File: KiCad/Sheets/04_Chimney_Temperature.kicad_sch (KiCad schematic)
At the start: 2 parts, among them U3 MAX6675

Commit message: Footprints are created and assigned
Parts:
- U3: footprint (none) -> Connector_PinSocket_2.54mm:PinSocket_1x05_P2.54mm_Vertical
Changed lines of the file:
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@@
 		(exclude_from_sim no)
 		(in_bom yes)
-		(on_board yes)
+		(on_board no)
 		(in_pos_files yes)
 		(dnp no)
@@
 			)
 		)
-		(property "Footprint" ""
+		(property "Footprint" "Connector_PinSocket_2.54mm:PinSocket_1x05_P2.54mm_Vertical"
 			(at 139.7 95.25 0)
 			(hide yes)

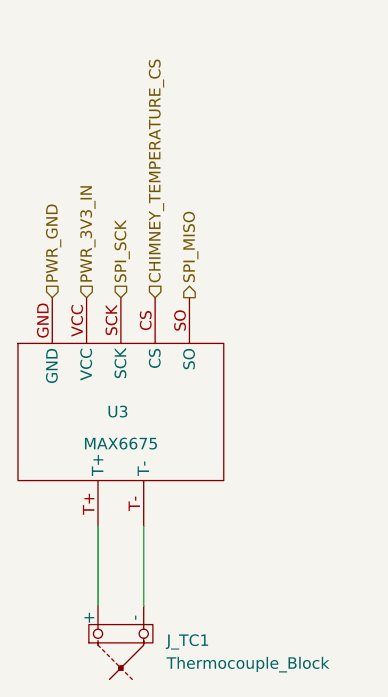
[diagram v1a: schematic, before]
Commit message: LEDs sheet added, schematic finished
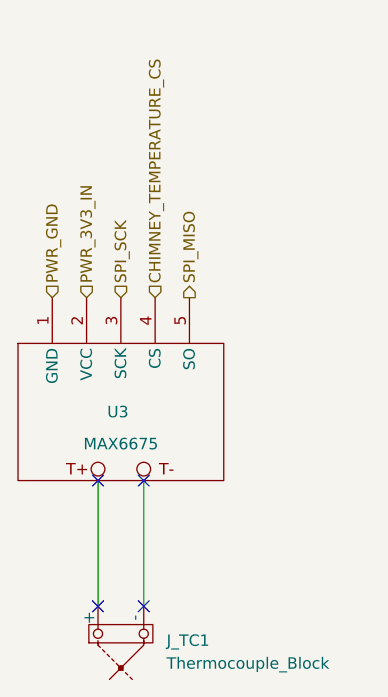
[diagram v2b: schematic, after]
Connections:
- net CHIMNEY_TEMPERATURE_CS: now also U3.4 (CS); no longer U3.CS
- net PWR_3V3_IN: now also U3.2 (VCC); no longer U3.VCC
- net PWR_GND: now also U3.1 (GND); no longer U3.GND
- net SPI_MISO: now also U3.5 (SO); no longer U3.SO
- net SPI_SCK: now also U3.3 (SCK); no longer U3.SCK
- net at J_TC1.1 (+): no longer U3.T+
- net at J_TC1.2 (-): no longer U3.T-
- no-connect marks 0 -> 4
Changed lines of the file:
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@@
 	(generator_version "10.0")
 	(paper "A4")
+	(no_connect
+		(at 137.16 102.87)
+	)
+	(no_connect
+		(at 137.16 116.84)
+	)
+	(no_connect
+		(at 142.24 116.84)
+	)
+	(no_connect
+		(at 142.24 102.87)
+	)
 	(wire
 		(pts
-			(xy 142.24 116.84) (xy 142.24 107.95)
+			(xy 142.24 102.87) (xy 142.24 116.84)
 		)
 		(stroke
@@
 	(wire
 		(pts
-			(xy 137.16 116.84) (xy 137.16 107.95)
+			(xy 137.16 102.87) (xy 137.16 116.84)
 		)
 		(stroke
@@
 			)
 		)
-		(pin "SCK"
-		)
-		(pin "SO"
-		)
-		(pin "CS"
-		)
-		(pin "VCC"
-		)
-		(pin "GND"
-		)
-		(pin "T-"
-		)
-		(pin "T+"
+		(pin "1"
+		)
+		(pin "5"
+		)
+		(pin "3"
+		)
+		(pin "2"
+		)
+		(pin "4"
 		)
 		(instances
